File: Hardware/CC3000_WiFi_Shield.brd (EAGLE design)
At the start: 69.8 x 53.3 mm, 32 parts, among them J1 U.FL, U2 ARDUINO_SHIELDLABEL, U3 74HC4050, U4 USD-SOCKETNEW, U5 CC3000

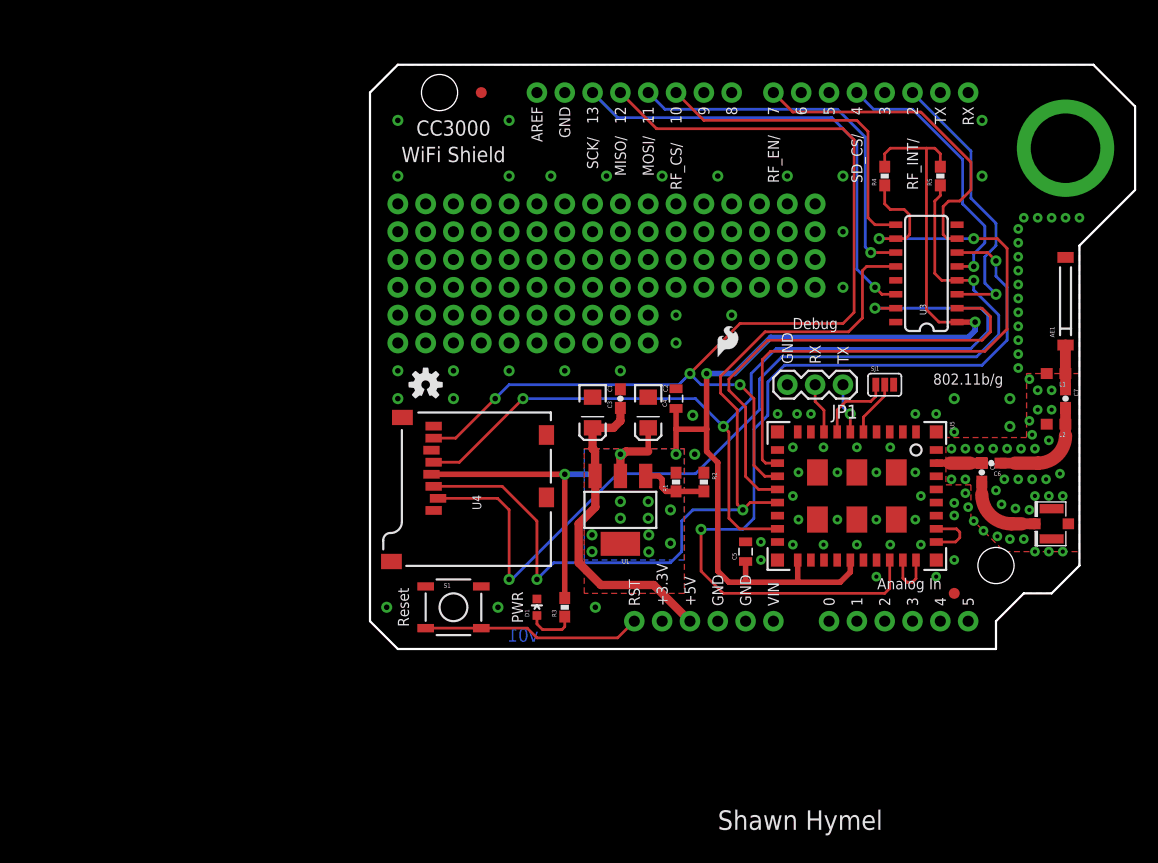
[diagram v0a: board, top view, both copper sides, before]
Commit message: Added high-Z protection on MISO, replaced tantalums, added 2nd set of headers on shield
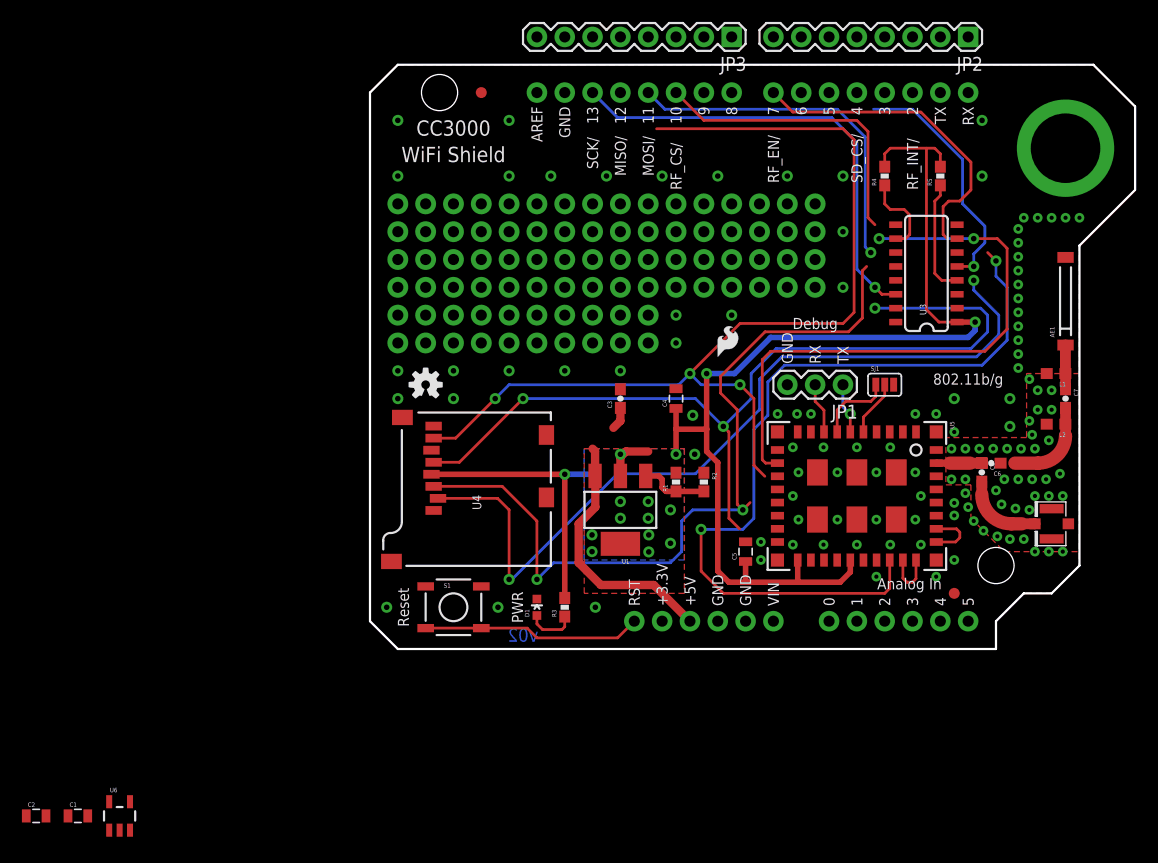
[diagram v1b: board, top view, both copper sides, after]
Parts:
- added JP2, JP3: (no value), SparkFun-Connectors:1X08
- added U6: 74AHC1G125, SparkFun-DigitalIC:SOT23-5
- C1, C2: device SparkFun-Capacitors:EIA3216 -> SparkFun-Capacitors:0805
- moved C2 66.9 mm to (-30.5, -15.2), turned to 0 degrees
- moved C1 59.7 mm to (-26.7, -15.2), turned to 0 degrees
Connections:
- net SD_CS renamed SD_CS_3.3V
- net SPI_MOSI renamed MOSI_3.3V
- net SPI_SCK renamed SCK_3.3V
- net WIFI_EN renamed EN_3.3V
- removed net D10: U2.D10, U3.9
- removed net D11: U2.D11, U3.11
- removed net D13: U2.D13, U3.14
- removed net D2: U2.D2, U3.3
- removed net D4: U2.D4, U3.5
- removed net D7: U2.D7, U3.7
- removed net SPI_MISO: U2.D12, U4.7, U5.P$13
- removed net WIFI_CS: R4.1, U3.10, U5.P$12
- removed net WIFI_INT: U3.2, U5.P$14
- new net AREF: JP3.8, U2.AREF
- new net EN_5V: JP2.8, U2.D7, U3.7
- new net INT_3.3V: JP2.3, U2.D2, U5.P$14
- new net MISO_3.3V: JP3.5, U2.D12, U4.7, U6.4
- new net MOSI_5V: JP3.4, U2.D11, U3.11
- new net N$125: JP2.1, U2.RX
- new net N$126: JP2.2, U2.TX
- new net N$127: JP2.4, U2.D3
- new net N$128: JP2.6, U2.D5
- new net N$129: JP2.7, U2.D6
- new net N$130: JP3.1, U2.D8
- new net N$131: JP3.2, U2.D9
- new net SCK_5V: JP3.6, U2.D13, U3.14
- new net SD_CS_5V: JP2.5, U2.D4, U3.5
- new net WIFI_CS_3.3V: R4.1, U3.10, U5.P$12, U6.1
- new net WIFI_CS_5V: JP3.3, U2.D10, U3.9
- new net WIFI_MISO: U5.P$13, U6.2
- net 3.3V: now also C2.1, U6.5; no longer C2.A
- net 5V: now also C1.1; no longer C1.A
- net GND: now also C1.2, C2.2, JP3.7, U6.3; no longer C1.C, C2.C
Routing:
- net SPI_MISO: track 97.5 -> 0.00 mm, vias 3 -> 0
- net MISO_3.3V: track 0.00 -> 91.6 mm, vias 0 -> 3
- net WIFI_CS: track 62.7 -> 0.00 mm, vias 2 -> 0
- net WIFI_CS_3.3V: track 0.00 -> 61.2 mm, vias 0 -> 2
- net WIFI_INT: track 43.3 -> 0.00 mm
- net D13: track 42.3 -> 0.00 mm, vias 1 -> 0
- net SCK_5V: track 0.00 -> 42.1 mm, vias 0 -> 1
- net D11: track 34.5 -> 0.00 mm, vias 1 -> 0
- net MOSI_5V: track 0.00 -> 32.2 mm, vias 0 -> 1
- net D7: track 30.3 -> 0.00 mm
- net D10: track 29.7 -> 0.00 mm
- net EN_5V: track 0.00 -> 29.5 mm
- net WIFI_CS_5V: track 0.00 -> 27.8 mm
- net D2: track 26.0 -> 0.00 mm, vias 1 -> 0
- net D4: track 24.7 -> 0.00 mm, vias 1 -> 0
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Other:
- board text added: "v02"
- board text removed: "v01"

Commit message: Made corrections to schematic/board from first prototype
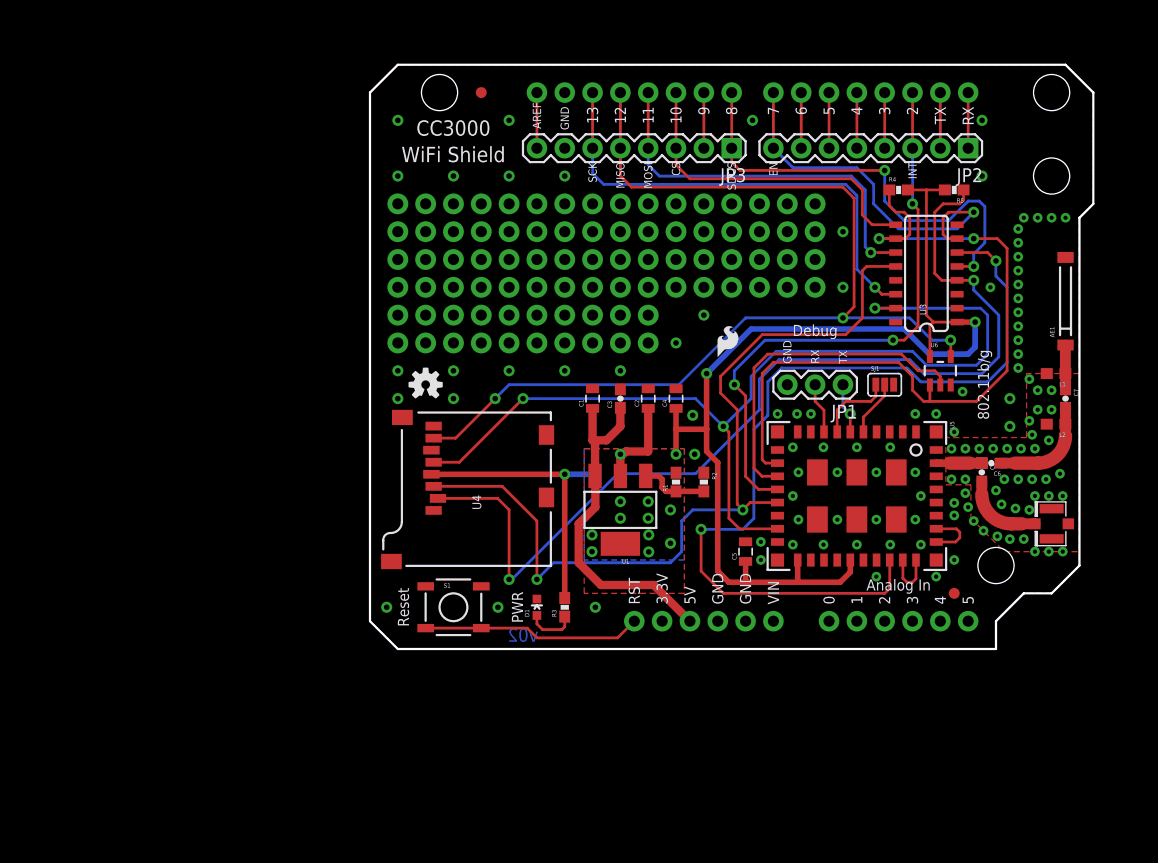
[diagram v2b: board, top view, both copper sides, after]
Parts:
- added STANDOFF1, STANDOFF2: STAND-OFF, SparkFun-Electromechanical:STAND-OFF
- U2: value ARDUINO_SHIELDLABEL -> ARDUINO_SHIELDNOLABELS; device SparkFun-Boards:DUEMILANOVE_SHIELD -> SparkFun-Boards:DUEMILANOVE_SHIELD_NOLABELS
- moved U6 85.2 mm to (52.1, 25.4)
- moved C2 67.6 mm to (25.4, 22.9), turned to 90 degrees
- moved C1 60.5 mm to (20.3, 22.9), turned to 90 degrees
- moved JP2 10.2 mm to (54.6, 45.7)
- moved JP3 10.2 mm to (33.0, 45.7)
- moved R5 1.80 mm to (53.3, 41.9), turned to 180 degrees
- moved R4 1.80 mm to (48.3, 41.9), turned to 0 degrees
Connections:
- net WIFI_CS_3.3V renamed CS_3.3V
- net WIFI_CS_5V renamed CS_5V
- net N$130: now also JP2.5, U2.D4; no longer JP3.1, U2.D8
- net SD_CS_5V: now also JP3.1, U2.D8; no longer JP2.5, U2.D4
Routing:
- net INT_3.3V: track 0.00 -> 53.5 mm, vias 0 -> 3
- net WIFI_MISO: track 0.00 -> 30.8 mm
- net SD_CS_5V: track 22.6 -> 41.7 mm, vias 1 -> 2
- net SCK_3.3V: track 81.0 -> 88.4 mm
- net CS_3.3V: track 61.2 -> 68.5 mm
- net 5V: track 25.6 -> 31.9 mm
- net MOSI_3.3V: track 73.1 -> 78.3 mm
- net SD_CS_3.3V: track 85.3 -> 90.4 mm
- net N$131: track 0.00 -> 5.08 mm
- net N$130: track 0.00 -> 5.08 mm
- net N$129: track 0.00 -> 5.08 mm
- net N$128: track 0.00 -> 5.08 mm
- net N$127: track 0.00 -> 5.08 mm
- net N$126: track 0.00 -> 5.08 mm
- net N$125: track 0.00 -> 5.08 mm
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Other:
- board size 69.8 x 53.3 mm -> 66 x 53.3 mm
- board text added: "0"
- board text added: "1"
- board text added: "10"
- board text added: "11"
- board text added: "12"
- board text added: "13"
- board text added: "2"
- board text added: "3"
- board text added: "3.3V"
- board text added: "4"
- board text added: "5"
- board text added: "5V"
- board text added: "6"
- board text added: "7"
- board text added: "8"
- board text added: "9"
- board text added: "AREF"
- board text added: "Analog In"
- board text added: "CS"
- board text added: "EN"
- board text added: "INT"
- board text added: "MISO"
- board text added: "MOSI"
- board text added: "RST"
- board text added: "SCK"
- board text added: "SDCS"
- board text added: "VIN"
- board text removed: "MISO/"
- board text removed: "MOSI/"
- board text removed: "RF_CS/"
- board text removed: "RF_EN/"
- board text removed: "RF_INT/"
- board text removed: "SCK/"
- board text removed: "SD_CS/"
